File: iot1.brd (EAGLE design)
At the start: 160 x 100 mm, 10 parts, among them U2 HTU21D

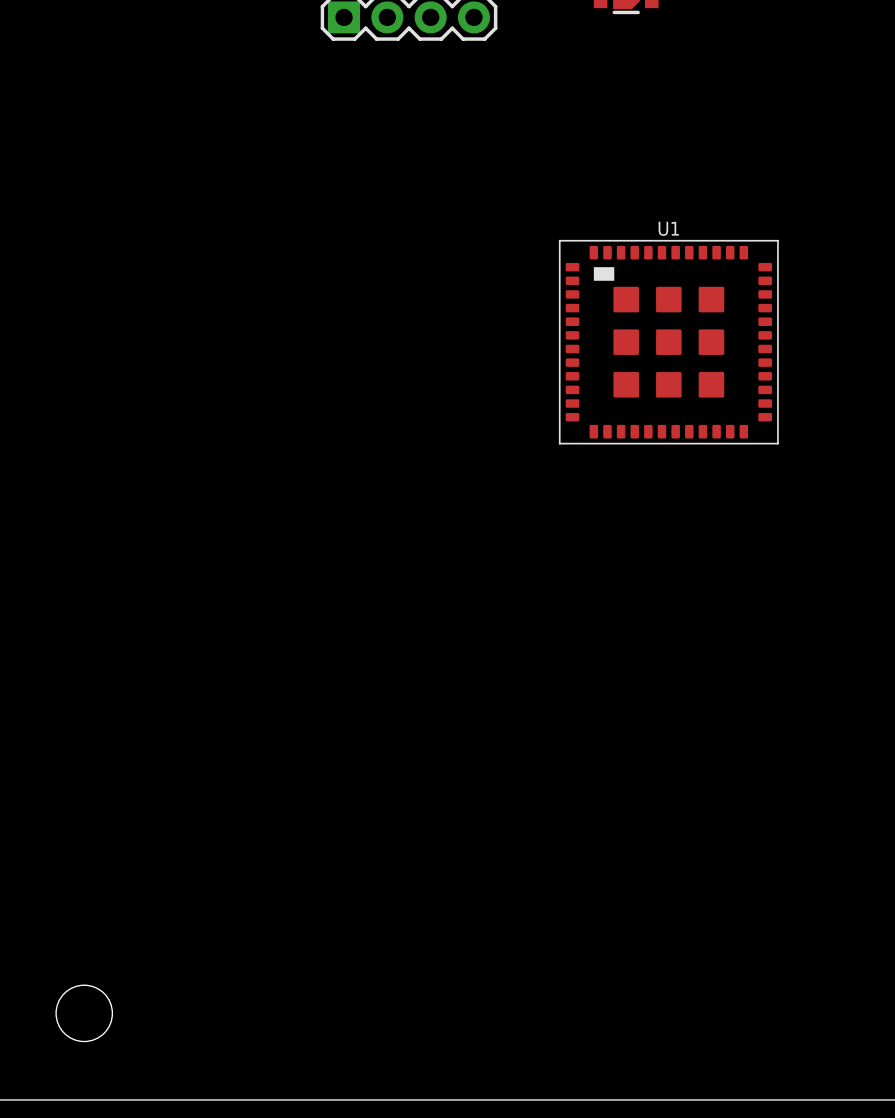
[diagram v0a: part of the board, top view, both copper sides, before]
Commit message: adding MEGA8-P controller
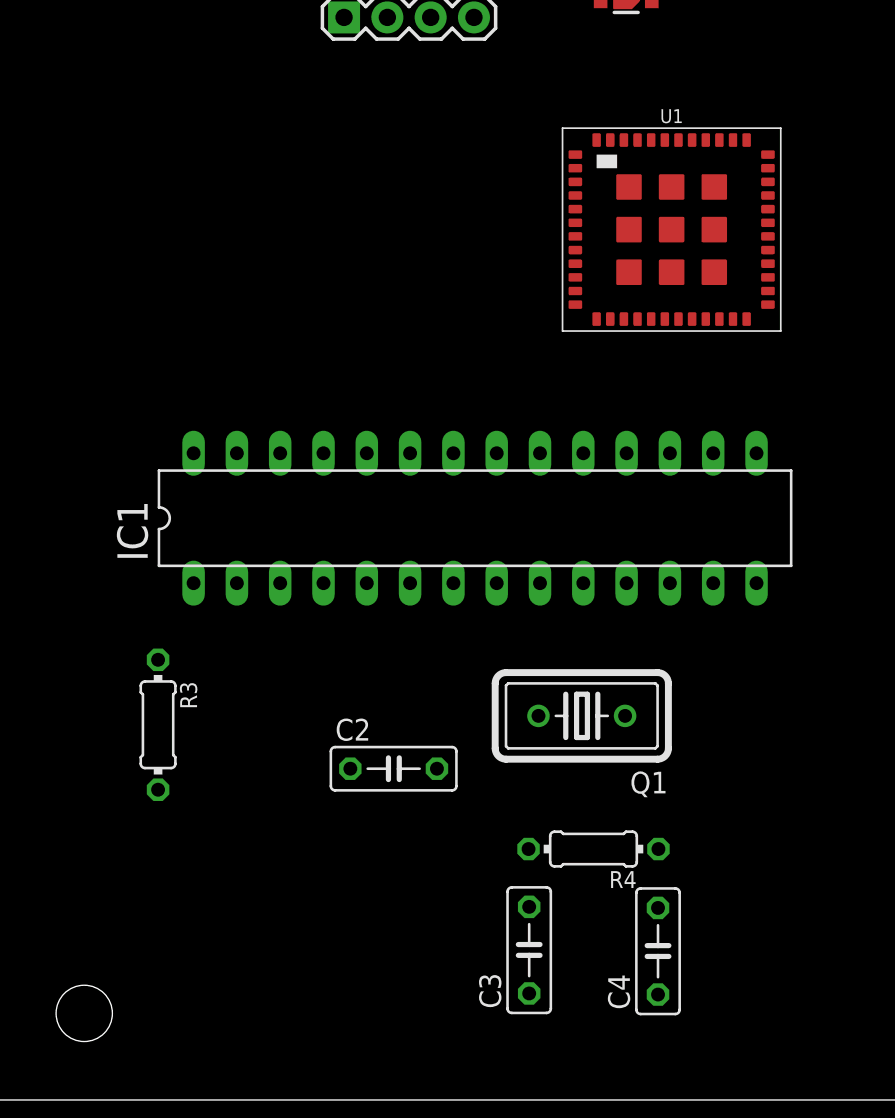
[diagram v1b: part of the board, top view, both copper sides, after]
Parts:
- added C2, C3, C4: (no value), rcl:C050-025X075
- added IC1: MEGA8-P, atmel:DIL28-3
- added Q1: (no value), crystal:HC18U-V
- added R3, R4: (no value), rcl:0204/7
- moved U1 6.61 mm to (39.5, 51.1)
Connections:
- new net 5V: C2.1, IC1.7, R3.2
- new net N$15: IC1.23
- new net N$16: IC1.24
- new net N$22: IC1.25
- new net N$23: IC1.26
- new net N$29: IC1.27
- new net N$31: IC1.28
- new net N$41: IC1.2
- new net N$42: IC1.3
- new net N$43: IC1.4
- new net N$44: IC1.5
- new net N$45: IC1.6
- new net N$58: IC1.11
- new net N$59: IC1.12
- new net N$60: IC1.13
- new net N$61: IC1.14
- new net N$62: IC1.15
- new net N$63: IC1.16
- new net N$64: IC1.17
- new net N$65: IC1.18
- new net N$66: IC1.19
- new net N$67: IC1.1, R3.1
- new net N$68: IC1.22
- new net N$69: IC1.21
- new net N$70: IC1.20
- new net N$72: C4.2, IC1.10, Q1.1, R4.1
- new net N$73: C3.2, IC1.9, Q1.2, R4.2
- net GND: now also C2.2, C3.1, C4.1, IC1.8

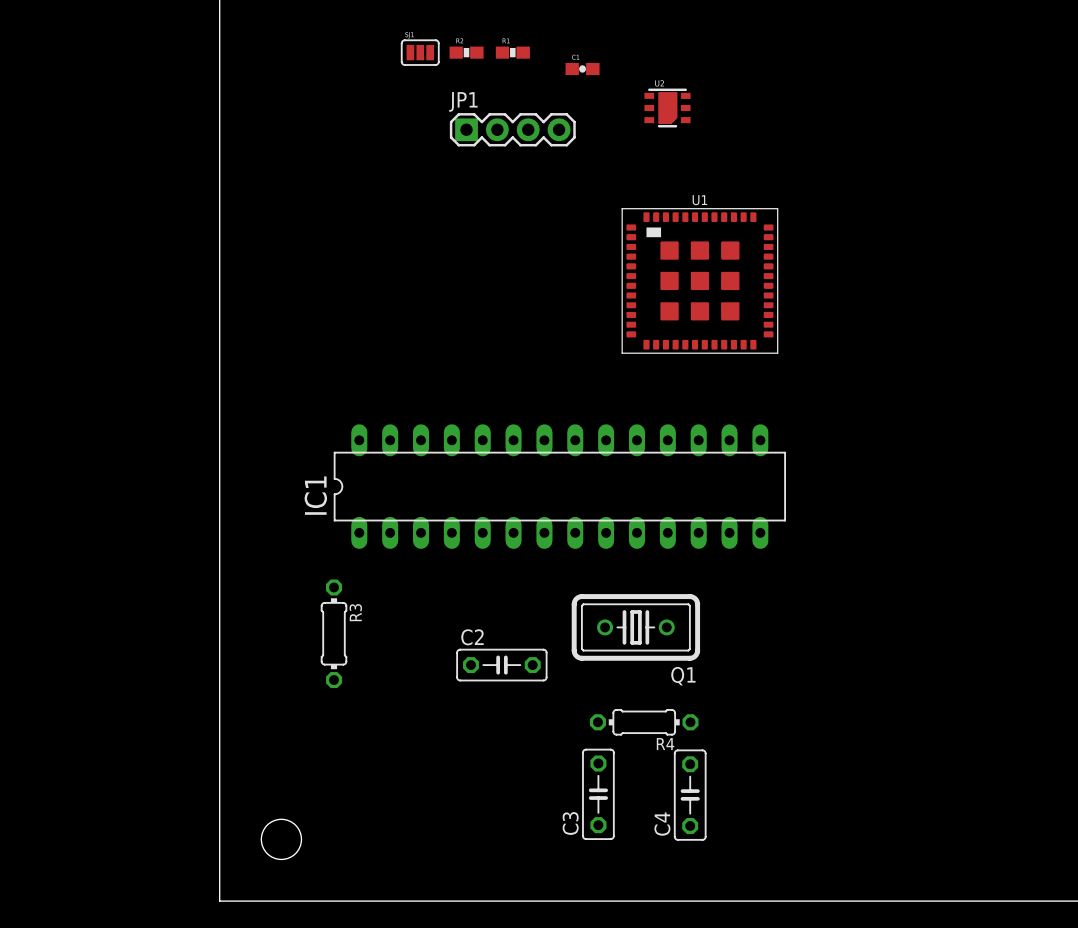
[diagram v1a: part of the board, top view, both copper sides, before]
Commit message: adding moisture input and adding voltage regulator
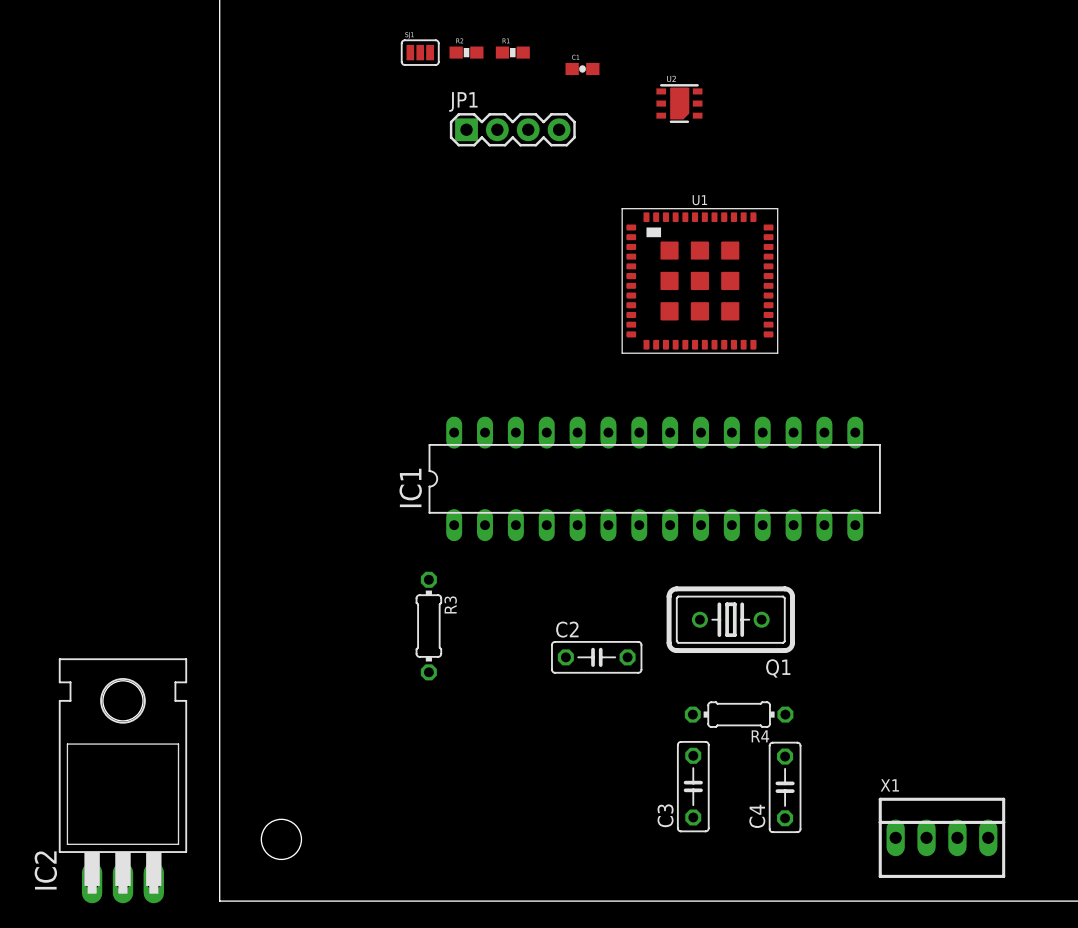
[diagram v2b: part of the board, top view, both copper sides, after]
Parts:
- added IC2: 7805T, linear:TO220H
- added X1: 22-23-2041, con-molex:22-23-2041
- moved IC1 7.84 mm to (35.8, 34.8)
- moved R3 7.84 mm to (17.2, 22.6)
- moved C2 7.84 mm to (31.0, 20.1)
- moved C3 7.84 mm to (39.0, 9.42)
- moved C4 7.84 mm to (46.5, 9.36)
- moved Q1 7.84 mm to (42.1, 23.2)
- moved R4 7.84 mm to (42.8, 15.4)
- moved U2 1.04 mm to (37.8, 65.7)
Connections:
- removed net N$65: IC1.18
- removed net N$66: IC1.19
- new net SOIL_MOISTURE_0: X1.1
- new net SOIL_MOISTURE_1: X1.3
- new net V_IN: IC2.1
- net 5V: now also IC2.3
- net GND: now also IC2.2, X1.2, X1.4
- net RX: now also IC1.18
- net TX: now also IC1.19

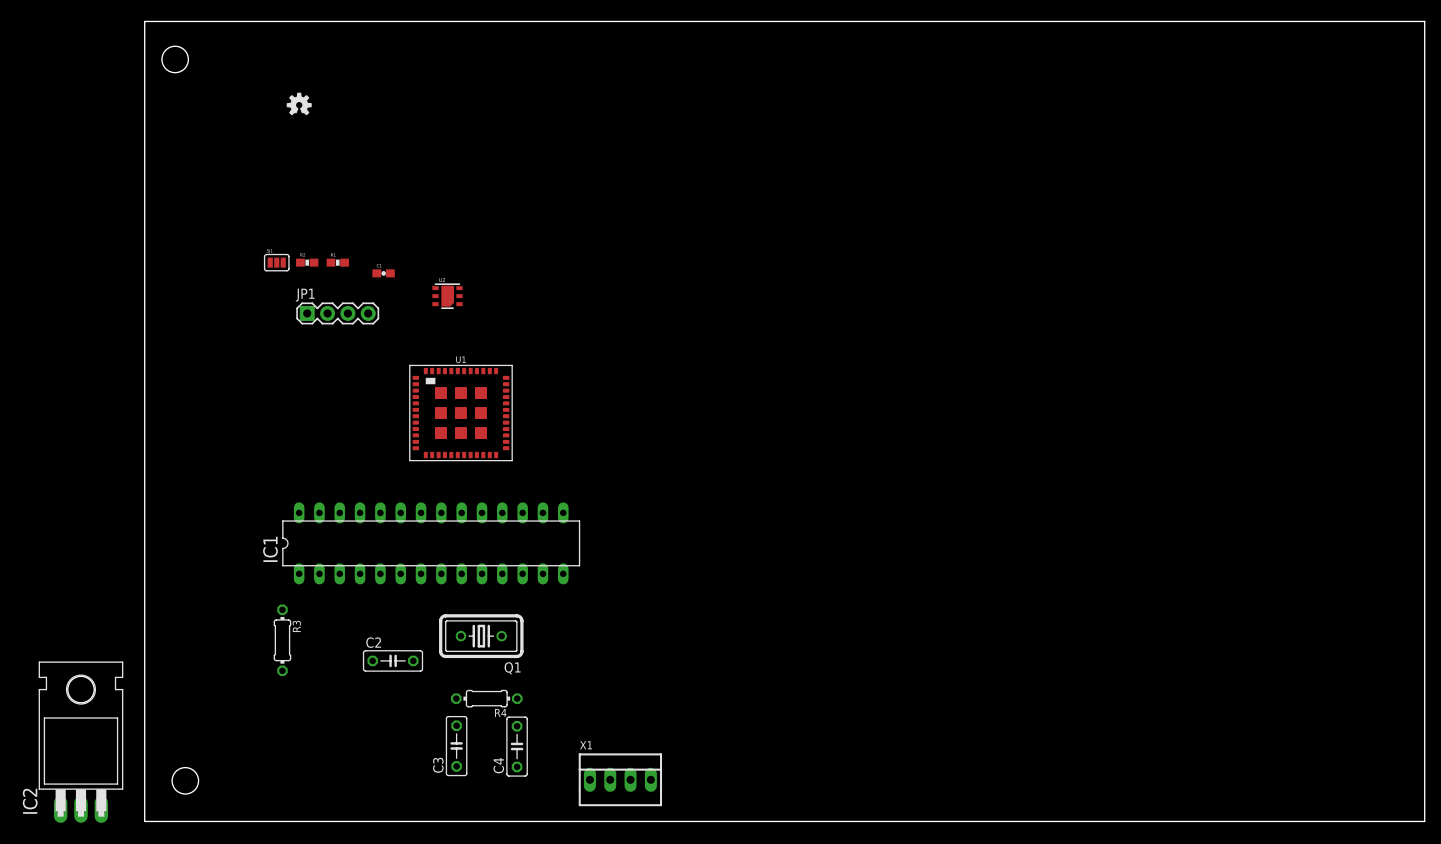
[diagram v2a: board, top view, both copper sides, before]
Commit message: adding power supply
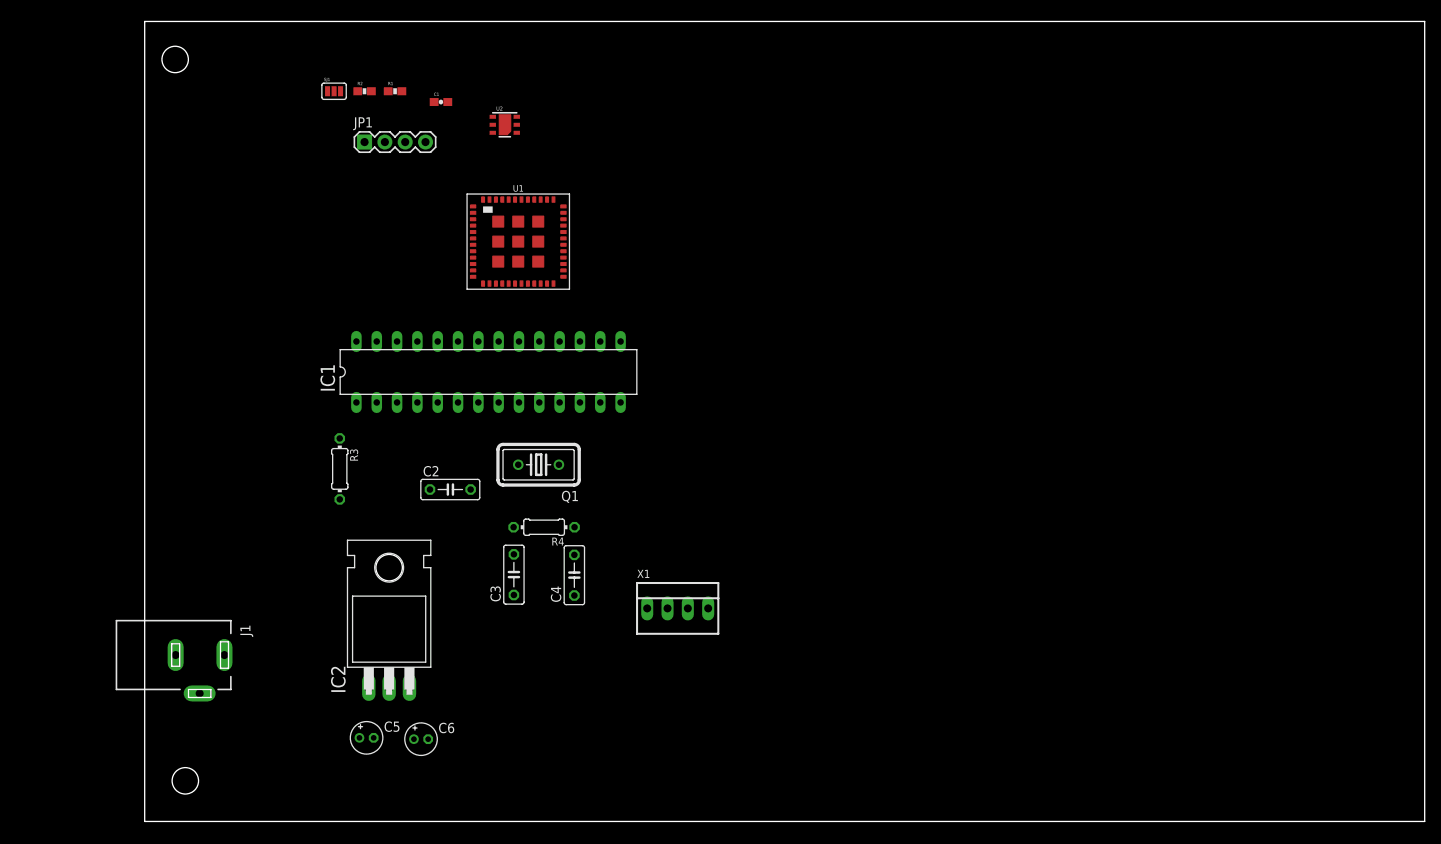
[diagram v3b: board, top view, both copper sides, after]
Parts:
- removed LOGO2: OSHW-LOGOS, SparkFun-Aesthetics:OSHW-LOGO-S
- added C5, C6: (no value), rcl:E1,8-4
- added J1: DCJ0202, con-jack:DCJ0202
- moved IC2 41.4 mm to (30.6, 26.9)
- moved C1 22.6 mm to (37.0, 89.9)
- moved R1 22.6 mm to (31.3, 91.3)
- moved R2 22.6 mm to (27.5, 91.3)
- moved SJ1 22.6 mm to (23.7, 91.3)
- moved C2 22.6 mm to (38.2, 41.5)
- moved C3 22.6 mm to (46.2, 30.8)
- moved C4 22.6 mm to (53.7, 30.8)
- moved IC1 22.6 mm to (43.0, 56.2)
- moved Q1 22.6 mm to (49.2, 44.6)
- moved R3 22.6 mm to (24.4, 44.1)
- moved R4 22.6 mm to (49.9, 36.8)
- moved U2 22.6 mm to (45.0, 87.1)
- moved X1 22.6 mm to (66.6, 26.6)
- moved JP1 22.6 mm to (27.5, 84.9)
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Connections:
- net 5V: now also C6.+
- net GND: now also C5.-, C6.-, J1.2, J1.3
- net V_IN: now also C5.+, J1.1

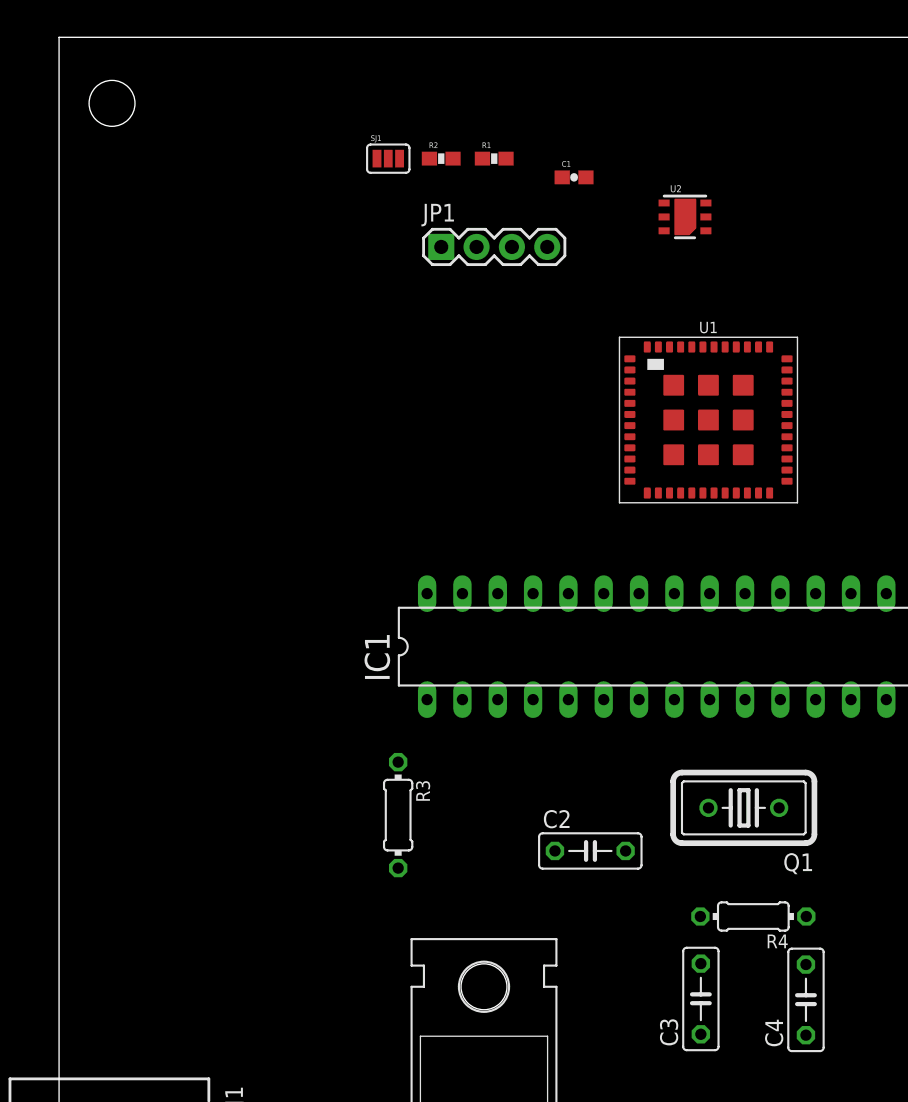
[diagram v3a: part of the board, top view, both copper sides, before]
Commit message: antena, power supply y conexiones lorawan
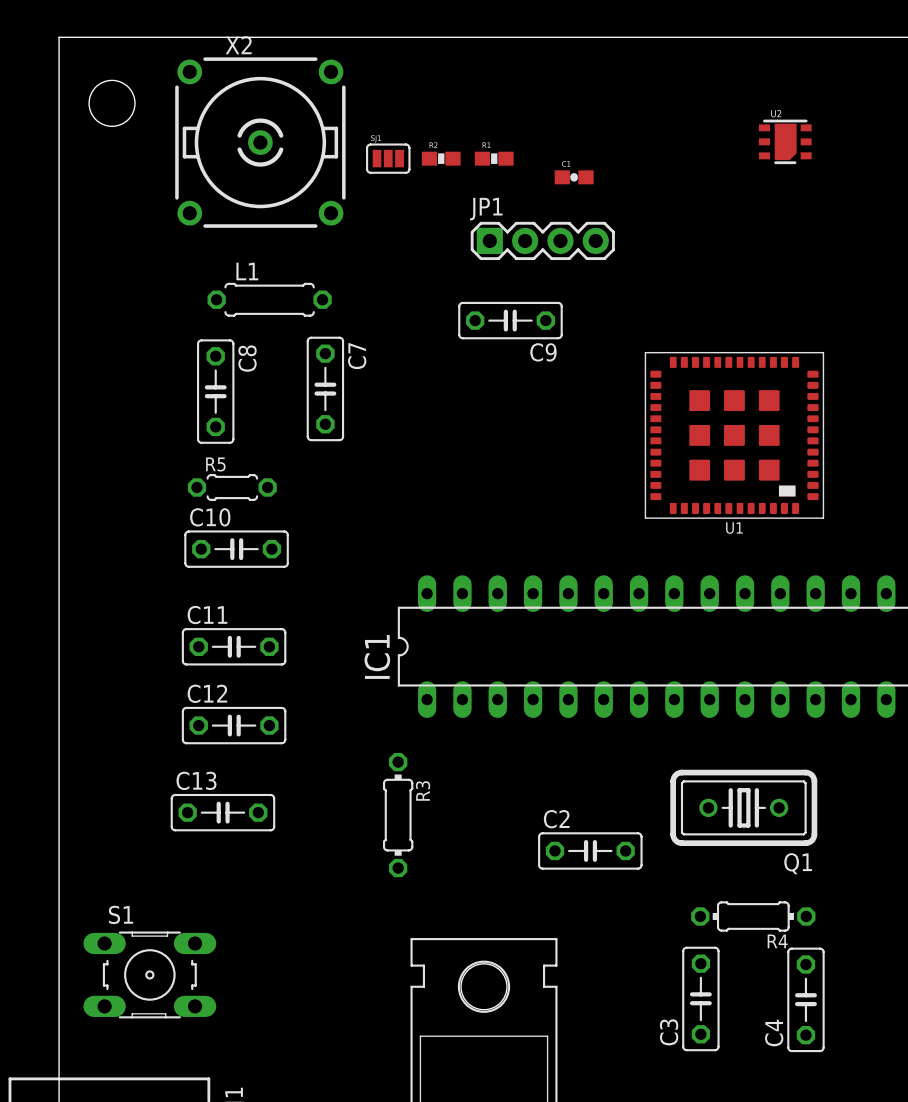
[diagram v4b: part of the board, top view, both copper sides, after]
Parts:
- added C10, C13: 0.1u, rcl:C050-025X075
- added C11, C9: 1u, rcl:C050-025X075
- added C12: 10u, rcl:C050-025X075
- added C7, C8: (no value), rcl:C050-025X075
- added L1: (no value), rcl:0207/7
- added R5: 10k, rcl:0204/5
- added S1: (no value), switch-omron:B3F-10XX
- added X2: A1944-50, con-coax:A1944
- moved U2 9.01 mm to (52.2, 92.5)
- moved JP1 3.52 mm to (31.0, 85.4)
- moved U1 2.17 mm to (48.6, 71.4), turned to 180 degrees
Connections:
- removed net N$36: U1.32
- removed net N$50: U1.44
- removed net N$6 (its old number): U1.7
- removed net N$7: U1.6
- removed net N$8: U1.5
- new net RF_LORAWAN: C7.2, L1.2, X2.1
- net 3.3V: now also C10.2, C11.2, C12.2, C9.2, U1.32, U1.5, U1.6
- net GND: now also C10.1, C11.1, C12.1, C13.1, C7.1, C8.1, C9.1, R5.1, S1.2, S1.3, S1.4, U1.44, U1.7, X2.2, X2.3, X2.4, X2.5
- net N$30: now also C8.2, L1.1
- net N$38: now also C13.2, S1.1
- net N$51: now also R5.2

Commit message: adc
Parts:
- added C14, C15: (no value), rcl:C0603
- added IC3: LTC2486C, linear-technology:DFN14-4X3
- moved C6 8.02 mm to (26.5, 9.78)
- moved IC2 7.30 mm to (23.3, 27.9)
- moved C5 6.09 mm to (21.7, 10.2)
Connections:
- removed net N$29: IC1.27
- new net N$71: IC3.11
- new net N$74: IC3.10
- new net N$75: IC3.9
- new net N$76: IC3.8
- new net N$77: IC3.7
- net 5V: now also C14.1, C15.1, IC3.12, IC3.13
- net GND: now also C14.2, C15.2, IC3.14, IC3.4, IC3.6, IC3.EXP
- net N$31: now also IC3.5; no longer IC1.28
- net SCL: now also IC1.28, IC3.1, IC3.3
- net SDA: now also IC1.27, IC3.2
